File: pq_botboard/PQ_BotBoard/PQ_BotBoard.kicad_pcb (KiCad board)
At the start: 6 copper layers, 64 x 52 mm, 31 parts, among them IC1 TCN75AVOA713, J1 53261-1471, J2 Conn_01x08_MountingPin, J3 53261-0271

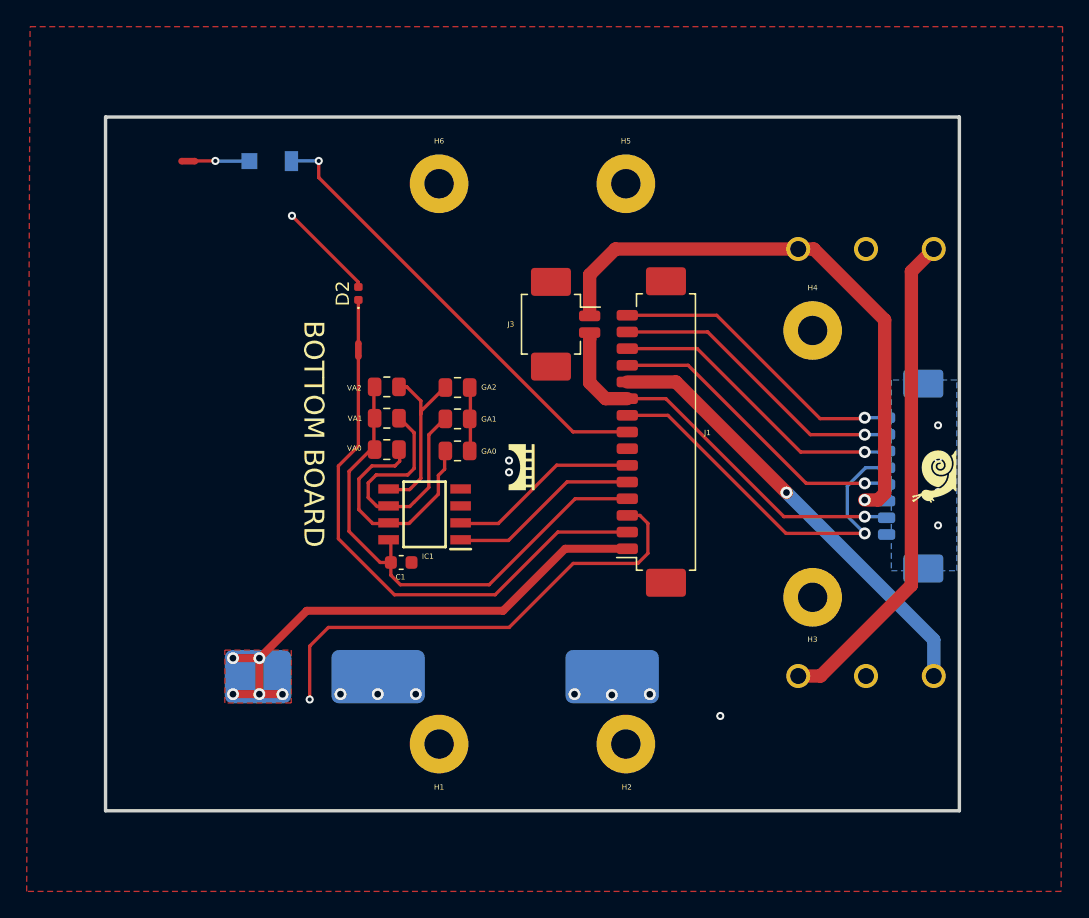
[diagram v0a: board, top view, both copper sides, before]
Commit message: Removed netie, updated SC footprint, trace reform, logo&name cleanup, footprint reconciled, DRC, centered umbilical connector
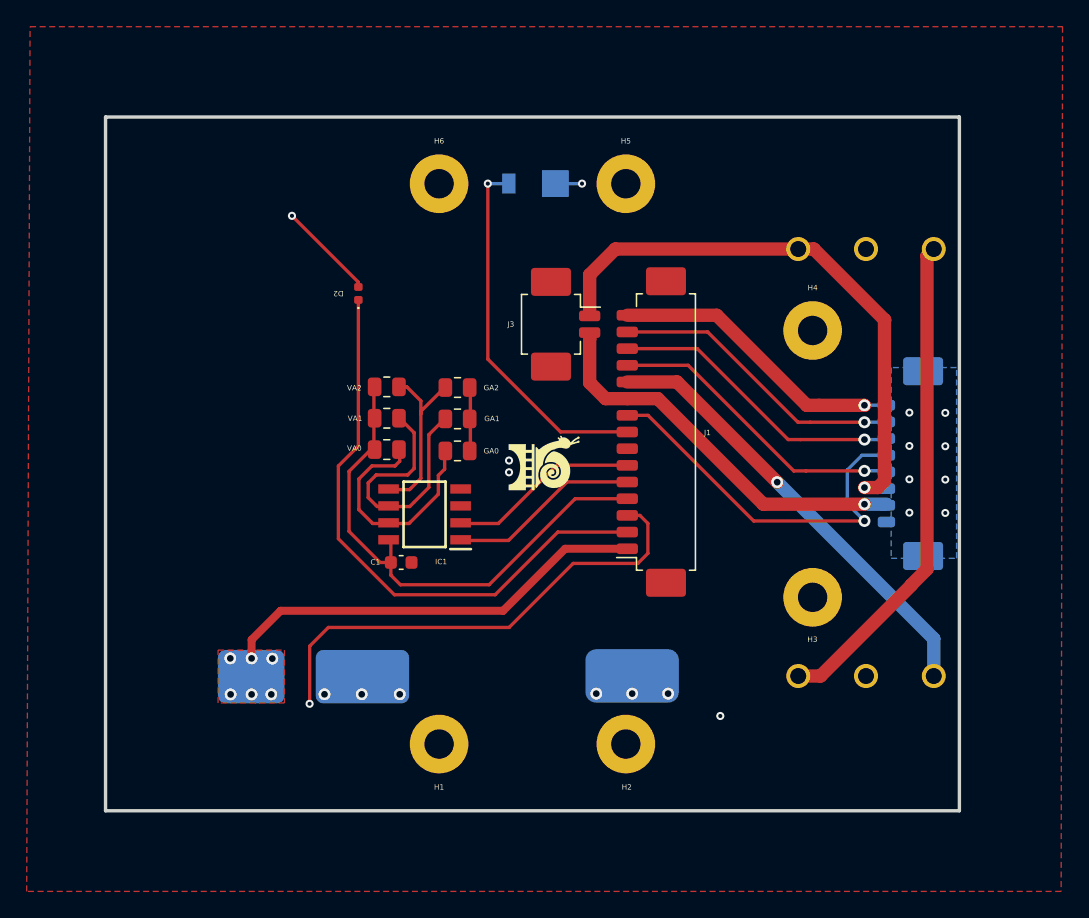
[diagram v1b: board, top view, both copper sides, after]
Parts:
- removed NT1, NT2: NetTie_2, NetTie:NetTie-2_SMD_Pad0.5mm
- added Annotation8: NSL_long, symbols-nsl:NSL-small, B.Cu at (75.5, 74.1)
- added Annotation9: NSL_hex, symbols-nsl:NSL_hexagon, B.Cu at (122.9, 56.9)
- Annotation1: value Silkscreen_Annotation -> GRSS; footprint -nsl_symbols:GRSS -> symbols-nsl:GRSS
- Annotation2: value Silkscreen_Annotation -> IEEE; footprint -nsl_symbols:IEEE_logo -> symbols-nsl:IEEE_logo
- Annotation3: value Silkscreen_Annotation -> UPC; footprint -nsl_symbols:UPC_positiu -> symbols-nsl:UPC_positiu
- Annotation4: value Silkscreen_Annotation -> Telecos; footprint -nsl_symbols:Telecos -> symbols-nsl:Telecos
- Annotation5: value Silkscreen_Annotation -> Bridgemaker; footprint -nsl_symbols:Bridgemaker -> symbols-nsl:Bridgemaker
- Annotation6: footprint symbols-nsl:snail -> symbols-nsl:Snail
- D1: footprint -nsl_passive:SLCD-61N8 -> passive-nsl:SLCD-61N8
- IC1: footprint -nsl_sensor:TCN75AVOA -> sensor-nsl:TCN75AVOA
- KS1: footprint -nsl_miscellaneous:D2FLA1 -> miscelaneous-nsl:D2FLA1
- KS2: footprint -nsl_miscellaneous:D2FLA -> miscelaneous-nsl:D2FLA
- SC1: footprint power-nsl:Lighttricity_S3040_CIC_ -> power-nsl:Lighttricity_S3040_CIC
- moved Annotation7 54.4 mm to (73.5, 73.9), turned to 90 degrees
- moved Annotation4 47.6 mm to (74.4, 60.6), turned to 90 degrees
- moved Annotation2 44.3 mm to (85.9, 35.2), turned to 0 degrees
- moved Annotation6 28.7 mm to (103.4, 57.6), turned to -90 degrees
- moved D1 20.2 mm to (102.1, 36.1), turned to 180 degrees
- moved Annotation1 15.5 mm to (85.1, 79.0), turned to 180 degrees
- moved Annotation3 5.16 mm to (73.8, 42.9), turned to 90 degrees
- moved J2 0.93 mm to (129.8, 57.0)
- turned GA0 to 0 degrees
- turned GA1 to 0 degrees
- turned GA2 to 0 degrees
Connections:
- D1 pad 2: /PH- -> GND
- D2 pad 1: Net-(D2-K) -> /MAG-Y
- GA0 pad 1: GND -> Net-(IC1-A0)
- GA0 pad 2: Net-(IC1-A0) -> GND
- GA1 pad 1: GND -> Net-(IC1-A1)
- GA1 pad 2: Net-(IC1-A1) -> GND
- GA2 pad 1: GND -> Net-(IC1-A2)
- GA2 pad 2: Net-(IC1-A2) -> GND
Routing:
- net /SOLAR_Y: track 39.4 -> 32.4 mm, vias 5 -> 6
- net /PH+: track 34.3 -> 27.5 mm
- net /MAG-Y: track 39.6 -> 43.9 mm
- net /PH-: track 4.09 -> 0.00 mm, vias 1 -> 0
- net Net-(D2-K): track 3.25 -> 0.00 mm
- net GND: track 4.75 -> 7.09 mm, vias 10 -> 15
- net /BATT+: track 44.2 -> 43.2 mm
- net /VCC_MAG: track 9686.7 -> 9687.4 mm
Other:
- board text added: "Adriano Camps Ştefan Podaru Guillem Gràcia Solá Marc Corretgé Artur Cot Arnau Dolz Edgar Hernández Roger Almirall Júlia Alós Óscar Pavón Nil Rius Júlia Tribó"
- board text removed: "BOTTOM BOARD"
- board text removed: "D1"
